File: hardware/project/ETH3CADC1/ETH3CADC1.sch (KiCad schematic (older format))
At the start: 2 parts

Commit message: PCB layout
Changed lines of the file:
@@
 $Descr A4 11693 8268
 encoding utf-8
-Sheet 1 13
+Sheet 1 15
 Title ""
 Date ""
@@
 $EndDescr
 $Sheet
-S 3450 1750 1350 1000
+S 2250 900  1350 1000
 U 5FD74AB8
 F0 "ADC 1" 50
 F1 "ADC1.sch" 50
-F2 "AD_COMP1" O R 4800 1850 50
-F3 "ADIN1" I L 3450 1850 50
-F4 "FGPA1_AD_IIN" I R 4800 1950 50
-F5 "FGPA1_AD_IRP" I R 4800 2050 50
-F6 "FGPA1_AD_ID" I R 4800 2150 50
-F7 "FGPA1_AD_IRN" I R 4800 2250 50
-F8 "VREF_N7V_LPF" I R 4800 2650 50
-F9 "VREF_N7V" I R 4800 2550 50
-F10 "VREF1_-7V" O L 3450 1950 50
-F11 "FPGA1_SW_VRH" I R 4800 2350 50
-$EndSheet
-$Sheet
-S 6500 1450 1800 1100
+F2 "AD_COMP1" O R 3600 1000 50
+F3 "ADIN1" I L 2250 1000 50
+F4 "FGPA1_AD_IIN" I R 3600 1100 50
+F5 "FGPA1_AD_IRP" I R 3600 1200 50
+F6 "FGPA1_AD_ID" I R 3600 1300 50
+F7 "FGPA1_AD_IRN" I R 3600 1400 50
+F8 "VREF_N7V_LPF" I R 3600 1800 50
+F9 "VREF_N7V" I R 3600 1700 50
+F10 "VREF1_-7V" O L 2250 1100 50
+F11 "FPGA1_SW_VRH" I R 3600 1500 50
+$EndSheet
+$Sheet
+S 7250 4550 1200 700
 U 600E050E
 F0 "VREF" 50
@@
 $EndSheet
 $Sheet
-S 3450 3000 1350 1000
+S 2250 2150 1350 1000
 U 602DC5A4
 F0 "ADC 2" 50
 F1 "ADC2.sch" 50
-F2 "FPGA2_SW_VRH" I R 4800 3600 50
-F3 "FGPA2_AD_IRN" I R 4800 3500 50
-F4 "FGPA2_AD_ID" I R 4800 3400 50
-F5 "FGPA2_AD_IRP" I R 4800 3300 50
-F6 "FGPA2_AD_IIN" I R 4800 3200 50
-F7 "ADIN2" I L 3450 3100 50
-F8 "AD_COMP2" O R 4800 3100 50
-F9 "VREF2_-7V" O L 3450 3200 50
-F10 "VREF_N7V" I R 4800 3800 50
-F11 "VREF_N7V_LPF" I R 4800 3900 50
-$EndSheet
-$Sheet
-S 6450 3300 1750 1150
+F2 "FPGA2_SW_VRH" I R 3600 2750 50
+F3 "FGPA2_AD_IRN" I R 3600 2650 50
+F4 "FGPA2_AD_ID" I R 3600 2550 50
+F5 "FGPA2_AD_IRP" I R 3600 2450 50
+F6 "FGPA2_AD_IIN" I R 3600 2350 50
+F7 "ADIN2" I L 2250 2250 50
+F8 "AD_COMP2" O R 3600 2250 50
+F9 "VREF2_-7V" O L 2250 2350 50
+F10 "VREF_N7V" I R 3600 2950 50
+F11 "VREF_N7V_LPF" I R 3600 3050 50
+$EndSheet
+$Sheet
+S 5250 900  1800 5350
 U 603BE5B9
 F0 "MCU" 50
 F1 "MCU.sch" 50
-$EndSheet
-$Sheet
-S 8850 3350 1200 1100
+F2 "RMII_TXD1" B R 7050 1000 50
+F3 "RMII_TXD0" B R 7050 1100 50
+F4 "RMII_TXEN" B R 7050 1200 50
+F5 "RMII_RXD0" B R 7050 1300 50
+F6 "RMII_RXD1" B R 7050 1400 50
+F7 "RMII_CRS_DV" B R 7050 1500 50
+F8 "RMII_MDIO" B R 7050 1600 50
+F9 "RMII_MDC" B R 7050 1700 50
+F10 "REF_CLK" B R 7050 1900 50
+F11 "NRST" B R 7050 1800 50
+F12 "TRIG_EN" O R 7050 2400 50
+F13 "TRIG_OUT" O R 7050 2500 50
+F14 "TRIG_IN" I R 7050 2600 50
+F15 "~CS" B R 7050 3300 50
+F16 "CKE" B R 7050 3400 50
+F17 "CLK" B R 7050 3500 50
+F18 "LDQM" B R 7050 3600 50
+F19 "UDQM" B R 7050 3700 50
+F20 "~WE" B R 7050 3800 50
+F21 "~CAS" B R 7050 3900 50
+F22 "~RAS" B R 7050 4000 50
+F23 "D[0..15]" B R 7050 4200 50
+F24 "A[0..12]" B R 7050 4100 50
+F25 "BA0" B R 7050 3100 50
+F26 "BA1" B R 7050 3200 50
+$EndSheet
+$Sheet
+S 7250 900  1200 1100
 U 603EFDDC
 F0 "Ethernet" 50
 F1 "Ethernet.sch" 50
-$EndSheet
-$Sheet
-S 8850 4850 1200 750
+F2 "TX+" B R 8450 1000 50
+F3 "TX-" B R 8450 1100 50
+F4 "RX+" B R 8450 1300 50
+F5 "RX-" B R 8450 1400 50
+F6 "RMII_TXD1" B L 7250 1000 50
+F7 "RMII_TXD0" B L 7250 1100 50
+F8 "RMII_TXEN" B L 7250 1200 50
+F9 "RMII_RXD0" B L 7250 1300 50
+F10 "RMII_RXD1" B L 7250 1400 50
+F11 "RMII_CRS_DV" B L 7250 1500 50
+F12 "RMII_MDIO" B L 7250 1600 50
+F13 "RMII_MDC" B L 7250 1700 50
+F14 "NRST" B L 7250 1800 50
+F15 "REF_CLK" B L 7250 1900 50
+$EndSheet
+$Sheet
+S 7250 2300 1200 400
 U 603FAFCE
 F0 "Trigger" 50
 F1 "Trigger.sch" 50
-$EndSheet
-$Sheet
-S 3450 4250 1350 1000
+F2 "EXT_TRIG" B R 8450 2400 50
+F3 "TRIG_EN" I L 7250 2400 50
+F4 "TRIG_OUT" I L 7250 2500 50
+F5 "TRIG_IN" O L 7250 2600 50
+$EndSheet
+$Sheet
+S 2250 3400 1350 1000
 U 605B3009
 F0 "ADC 3" 50
 F1 "ADC3.sch" 50
-F2 "FPGA3_SW_VRH" I R 4800 4850 50
-F3 "FGPA3_AD_IRN" I R 4800 4750 50
-F4 "FGPA3_AD_ID" I R 4800 4650 50
-F5 "FGPA3_AD_IRP" I R 4800 4550 50
-F6 "FGPA3_AD_IIN" I R 4800 4450 50
-F7 "ADIN3" I L 3450 4350 50
-F8 "AD_COMP3" O R 4800 4350 50
-F9 "VREF3_-7V" O L 3450 4450 50
-F10 "VREF_N7V" I R 4800 5050 50
-F11 "VREF_N7V_LPF" I R 4800 5150 50
-$EndSheet
-$Sheet
-S 5100 1750 1250 1000
+F2 "FPGA3_SW_VRH" I R 3600 4000 50
+F3 "FGPA3_AD_IRN" I R 3600 3900 50
+F4 "FGPA3_AD_ID" I R 3600 3800 50
+F5 "FGPA3_AD_IRP" I R 3600 3700 50
+F6 "FGPA3_AD_IIN" I R 3600 3600 50
+F7 "ADIN3" I L 2250 3500 50
+F8 "AD_COMP3" O R 3600 3500 50
+F9 "VREF3_-7V" O L 2250 3600 50
+F10 "VREF_N7V" I R 3600 4200 50
+F11 "VREF_N7V_LPF" I R 3600 4300 50
+$EndSheet
+$Sheet
+S 3800 900  1250 1000
 U 606766CF
 F0 "FPGA 1" 50
@@
 $EndComp
 $Sheet
-S 2000 1750 1100 1000
+S 800  900  1100 1000
 U 60C206FB
 F0 "CH1 Connector" 50
 F1 "CH1_CONN.sch" 50
-$EndSheet
-$Sheet
-S 2000 3000 1100 1000
+F2 "ADIN1" O R 1900 1000 50
+$EndSheet
+$Sheet
+S 800  2150 1100 1000
 U 60C24B76
 F0 "CH2 Connector" 50
@@
 $EndSheet
 $Sheet
-S 2000 4250 1100 1000
+S 800  3400 1100 1000
 U 60C27246
 F0 "CH3 Connector" 50
@@
 $EndSheet
 $Sheet
-S 8900 1450 1400 1100
+S 8650 900  1200 1800
 U 60F396AA
 F0 "Connector" 50
 F1 "Connector.sch" 50
+F2 "EXT_TRIG" B L 8650 2400 50
+F3 "TX+" B L 8650 1000 50
+F4 "TX-" B L 8650 1100 50
+F5 "RX+" B L 8650 1300 50
+F6 "RX-" B L 8650 1400 50
+$EndSheet
+Wire Wire Line
+	1900 1000 2250 1000
+$Sheet
+S 7250 3000 1200 1300
+U 60325873
+F0 "SDRAM" 50
+F1 "SDRAM.sch" 50
+F2 "BA0" B L 7250 3100 50
+F3 "BA1" B L 7250 3200 50
+F4 "~CS" B L 7250 3300 50
+F5 "CKE" B L 7250 3400 50
+F6 "CLK" B L 7250 3500 50
+F7 "LDQM" B L 7250 3600 50
+F8 "UDQM" B L 7250 3700 50
+F9 "~WE" B L 7250 3800 50
+F10 "~CAS" B L 7250 3900 50
+F11 "~RAS" B L 7250 4000 50
+F12 "A[0..12]" B L 7250 4100 50
+F13 "D[0..15]" B L 7250 4200 50
+$EndSheet
+Wire Wire Line
+	7250 1000 7050 1000
+Wire Wire Line
+	7050 1100 7250 1100
+Wire Wire Line
+	7250 1200 7050 1200
+Wire Wire Line
+	7050 1300 7250 1300
+Wire Wire Line
+	7250 1400 7050 1400
+Wire Wire Line
+	7050 1500 7250 1500
+Wire Wire Line
+	7250 1600 7050 1600
+Wire Wire Line
+	7050 1700 7250 1700
+Wire Wire Line
+	7250 1800 7050 1800
+Wire Wire Line
+	7050 1900 7250 1900
+Wire Wire Line
+	7250 2400 7050 2400
+Wire Wire Line
+	7050 2500 7250 2500
+Wire Wire Line
+	7050 2600 7250 2600
+Wire Wire Line
+	7250 3100 7050 3100
+Wire Wire Line
+	7050 3200 7250 3200
+Wire Wire Line
+	7250 3300 7050 3300
+Wire Wire Line
+	7050 3400 7250 3400
+Wire Wire Line
+	7250 3500 7050 3500
+Wire Wire Line
+	7050 3600 7250 3600
+Wire Wire Line
+	7250 3700 7050 3700
+Wire Wire Line
+	7050 3800 7250 3800
+Wire Wire Line
+	7250 3900 7050 3900
+Wire Wire Line
+	7050 4000 7250 4000
+Wire Bus Line
+	7250 4100 7050 4100
+Wire Bus Line
+	7050 4200 7250 4200
+Wire Wire Line
+	8450 1400 8650 1400
+Wire Wire Line
+	8650 1300 8450 1300
+Wire Wire Line
+	8450 1100 8650 1100
+Wire Wire Line
+	8650 1000 8450 1000
+Wire Wire Line
+	8450 2400 8650 2400
+$Sheet
+S 7250 5550 1200 700
+U 5FE6B116
+F0 "Power" 50
+F1 "Power.sch" 50
 $EndSheet
 $EndSCHEMATC

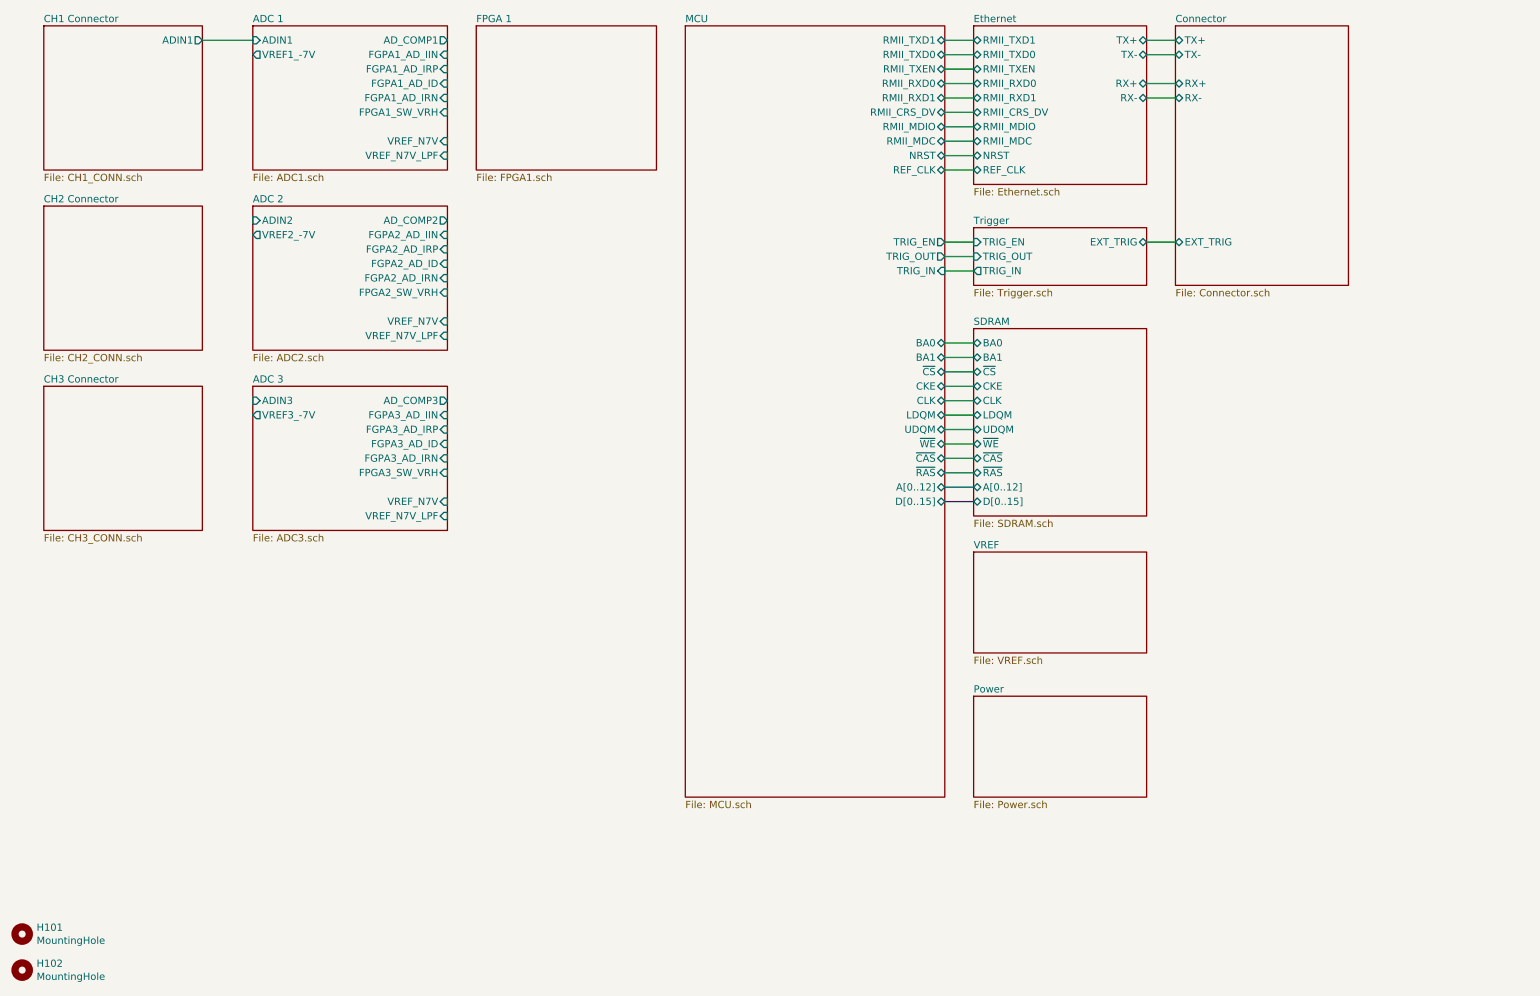
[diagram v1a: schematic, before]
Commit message: SDRAM works, thanks to the website https://medium.com/@pjinwoo123/stm32h7-external-sdram-evaluation-board-cc72444898d8 . Modified the code to work with SDRAM BANK2. SCPI library works.
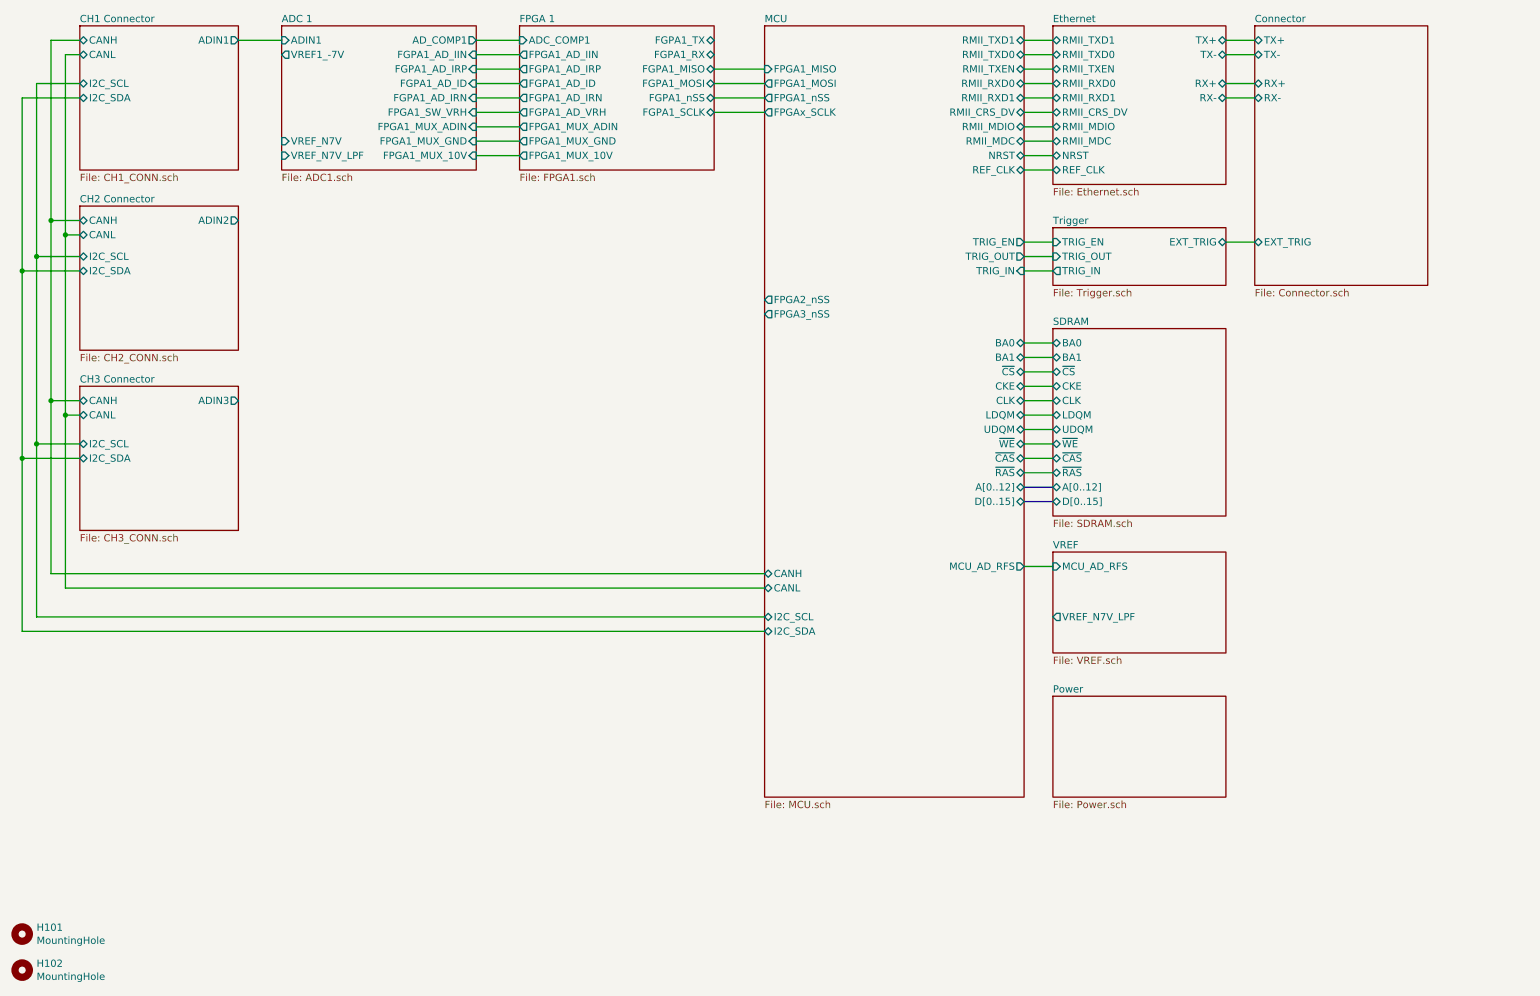
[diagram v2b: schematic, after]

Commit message: Added SDRAM to the linker file.
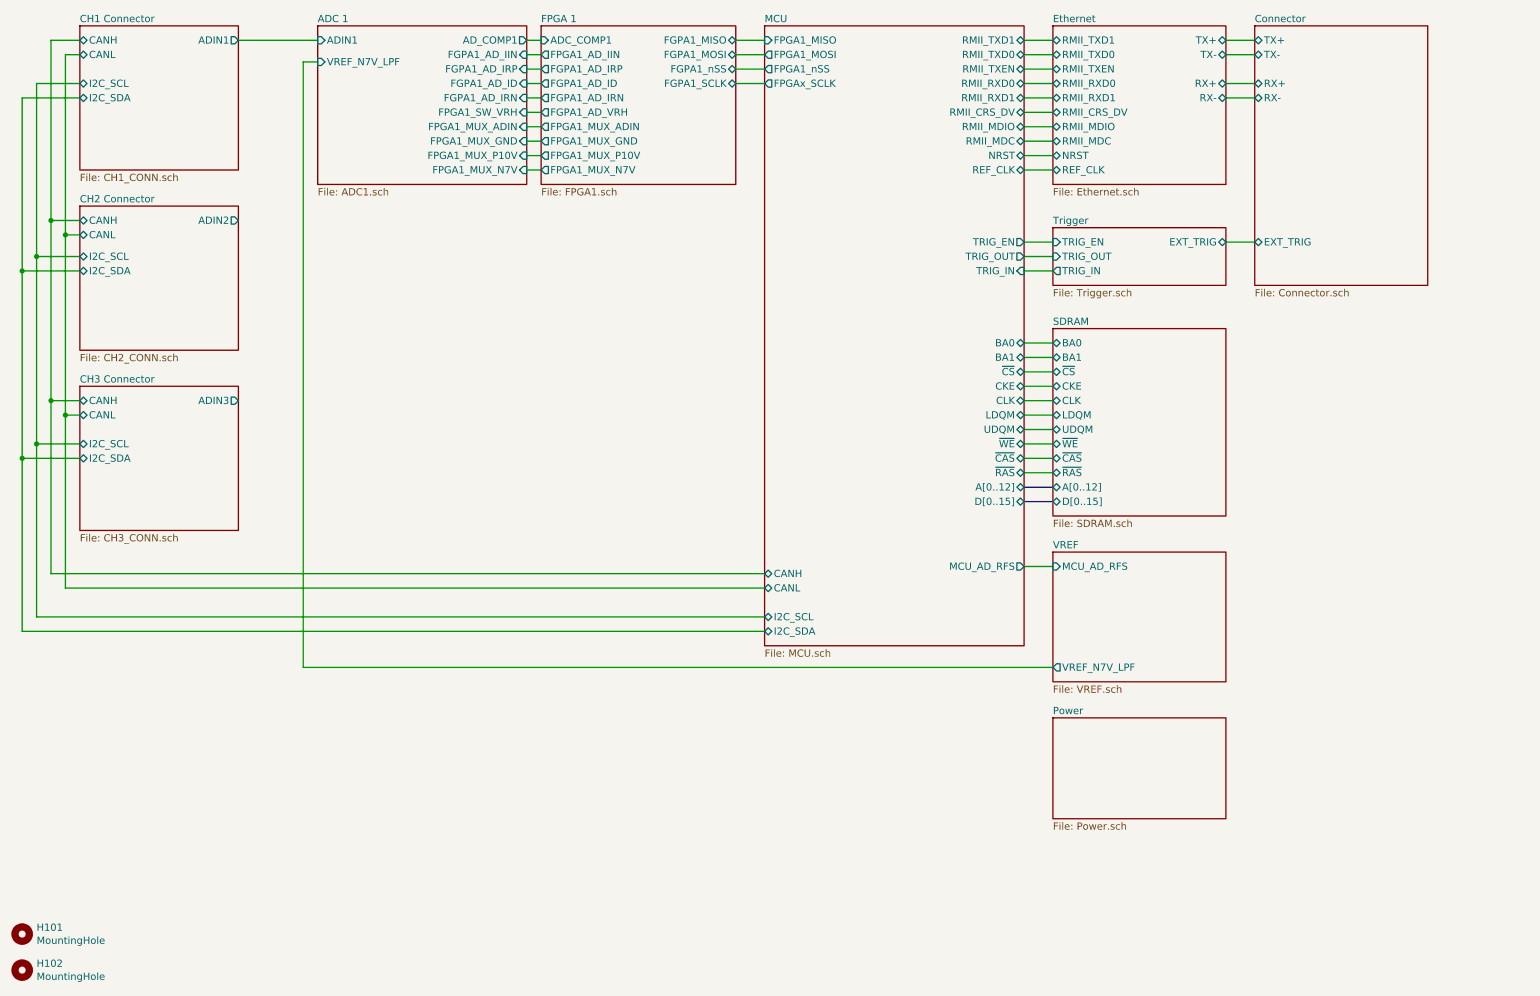
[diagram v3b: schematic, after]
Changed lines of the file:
@@
 $EndDescr
 $Sheet
-S 2450 900  1350 1000
+S 2700 900  1450 1100
 U 5FD74AB8
 F0 "ADC 1" 50
 F1 "ADC1.sch" 50
-F2 "AD_COMP1" O R 3800 1000 50
-F3 "ADIN1" I L 2450 1000 50
-F4 "FGPA1_AD_IIN" I R 3800 1100 50
-F5 "FGPA1_AD_IRP" I R 3800 1200 50
-F6 "FGPA1_AD_ID" I R 3800 1300 50
-F7 "FGPA1_AD_IRN" I R 3800 1400 50
-F8 "VREF_N7V_LPF" I L 2450 1800 50
-F9 "VREF_N7V" I L 2450 1700 50
-F10 "VREF1_-7V" O L 2450 1100 50
-F11 "FPGA1_SW_VRH" I R 3800 1500 50
-F12 "FPGA1_MUX_ADIN" I R 3800 1600 50
-F13 "FPGA1_MUX_GND" I R 3800 1700 50
-F14 "FPGA1_MUX_10V" I R 3800 1800 50
-$EndSheet
-$Sheet
-S 7800 4550 1200 700
+F2 "AD_COMP1" O R 4150 1000 50
+F3 "ADIN1" I L 2700 1000 50
+F4 "FGPA1_AD_IIN" I R 4150 1100 50
+F5 "FGPA1_AD_IRP" I R 4150 1200 50
+F6 "FGPA1_AD_ID" I R 4150 1300 50
+F7 "FGPA1_AD_IRN" I R 4150 1400 50
+F8 "VREF_N7V_LPF" I L 2700 1150 50
+F9 "FPGA1_SW_VRH" I R 4150 1500 50
+F10 "FPGA1_MUX_ADIN" I R 4150 1600 50
+F11 "FPGA1_MUX_GND" I R 4150 1700 50
+F12 "FPGA1_MUX_P10V" I R 4150 1800 50
+F13 "FPGA1_MUX_N7V" I R 4150 1900 50
+$EndSheet
+$Sheet
+S 7800 4550 1200 900
 U 600E050E
 F0 "VREF" 50
 F1 "VREF.sch" 50
-F2 "VREF_N7V_LPF" O L 7800 5000 50
+F2 "VREF_N7V_LPF" O L 7800 5350 50
 F3 "MCU_AD_RFS" I L 7800 4650 50
 $EndSheet
 $Sheet
-S 5800 900  1800 5350
+S 5800 900  1800 4300
 U 603BE5B9
 F0 "MCU" 50
@@
 F25 "BA0" B R 7600 3100 50
 F26 "BA1" B R 7600 3200 50
-F27 "FPGAx_SCLK" O L 5800 1500 50
-F28 "FPGA1_nSS" O L 5800 1400 50
+F27 "FPGAx_SCLK" O L 5800 1300 50
+F28 "FPGA1_nSS" O L 5800 1200 50
 F29 "I2C_SCL" B L 5800 5000 50
 F30 "I2C_SDA" B L 5800 5100 50
 F31 "CANH" B L 5800 4700 50
 F32 "CANL" B L 5800 4800 50
-F33 "FPGA1_MOSI" O L 5800 1300 50
-F34 "FPGA1_MISO" I L 5800 1200 50
-F35 "FPGA2_nSS" O L 5800 2800 50
-F36 "FPGA3_nSS" O L 5800 2900 50
-F37 "MCU_AD_RFS" O R 7600 4650 50
+F33 "FPGA1_MOSI" O L 5800 1100 50
+F34 "FPGA1_MISO" I L 5800 1000 50
+F35 "MCU_AD_RFS" O R 7600 4650 50
 $EndSheet
 $Sheet
@@
 $EndSheet
 Wire Wire Line
-	2150 1000 2450 1000
+	2150 1000 2700 1000
 $Sheet
 S 7800 3000 1200 1300
@@
 	9000 2400 9200 2400
 $Sheet
-S 7800 5550 1200 700
+S 7800 5700 1200 700
 U 5FE6B116
 F0 "Power" 50
@@
 $EndSheet
 Wire Wire Line
-	4100 1000 3800 1000
-Wire Wire Line
-	3800 1100 4100 1100
-Wire Wire Line
-	4100 1200 3800 1200
-Wire Wire Line
-	3800 1300 4100 1300
-Wire Wire Line
-	4100 1400 3800 1400
-Wire Wire Line
-	3800 1500 4100 1500
-Wire Wire Line
-	5450 1200 5800 1200
-Wire Wire Line
-	5800 1300 5450 1300
-Wire Wire Line
-	5450 1400 5800 1400
-Wire Wire Line
-	5800 1500 5450 1500
-Wire Wire Line
-	4100 1600 3800 1600
-Wire Wire Line
-	3800 1700 4100 1700
-Wire Wire Line
-	4100 1800 3800 1800
+	5600 1000 5800 1000
+Wire Wire Line
+	5800 1100 5600 1100
+Wire Wire Line
+	5600 1200 5800 1200
+Wire Wire Line
+	5800 1300 5600 1300
 $Sheet
 S 1050 3400 1100 1000
@@
 $EndSheet
 $Sheet
-S 4100 900  1350 1000
+S 4250 900  1350 1100
 U 606766CF
 F0 "FPGA 1" 50
 F1 "FPGA1.sch" 50
-F2 "FPGA1_AD_IIN" O L 4100 1100 50
-F3 "FGPA1_AD_IRN" O L 4100 1400 50
-F4 "FGPA1_AD_ID" O L 4100 1300 50
-F5 "FGPA1_AD_IRP" O L 4100 1200 50
-F6 "FGPA1_AD_VRH" O L 4100 1500 50
-F7 "ADC_COMP1" I L 4100 1000 50
-F8 "FGPA1_TX" B R 5450 1000 50
-F9 "FGPA1_RX" B R 5450 1100 50
-F10 "FGPA1_MISO" B R 5450 1200 50
-F11 "FGPA1_MOSI" B R 5450 1300 50
-F12 "FGPA1_nSS" B R 5450 1400 50
-F13 "FGPA1_SCLK" B R 5450 1500 50
-F14 "FPGA1_MUX_ADIN" O L 4100 1600 50
-F15 "FPGA1_MUX_GND" O L 4100 1700 50
-F16 "FPGA1_MUX_10V" O L 4100 1800 50
+F2 "FPGA1_AD_IIN" O L 4250 1100 50
+F3 "FGPA1_AD_IRN" O L 4250 1400 50
+F4 "FGPA1_AD_ID" O L 4250 1300 50
+F5 "FGPA1_AD_IRP" O L 4250 1200 50
+F6 "FGPA1_AD_VRH" O L 4250 1500 50
+F7 "ADC_COMP1" I L 4250 1000 50
+F8 "FGPA1_MISO" B R 5600 1000 50
+F9 "FGPA1_MOSI" B R 5600 1100 50
+F10 "FGPA1_nSS" B R 5600 1200 50
+F11 "FGPA1_SCLK" B R 5600 1300 50
+F12 "FPGA1_MUX_ADIN" O L 4250 1600 50
+F13 "FPGA1_MUX_GND" O L 4250 1700 50
+F14 "FPGA1_MUX_P10V" O L 4250 1800 50
+F15 "FPGA1_MUX_N7V" O L 4250 1900 50
 $EndSheet
 Wire Wire Line
@@
 	850  4700 850  3500
 Connection ~ 850  3500
+Wire Wire Line
+	4150 1900 4250 1900
+Wire Wire Line
+	4250 1800 4150 1800
+Wire Wire Line
+	4150 1700 4250 1700
+Wire Wire Line
+	4250 1600 4150 1600
+Wire Wire Line
+	4150 1500 4250 1500
+Wire Wire Line
+	4250 1400 4150 1400
+Wire Wire Line
+	4150 1300 4250 1300
+Wire Wire Line
+	4250 1200 4150 1200
+Wire Wire Line
+	4150 1100 4250 1100
+Wire Wire Line
+	4250 1000 4150 1000
+Wire Wire Line
+	7800 5350 2600 5350
+Wire Wire Line
+	2600 5350 2600 1150
+Wire Wire Line
+	2600 1150 2700 1150
 $EndSCHEMATC
